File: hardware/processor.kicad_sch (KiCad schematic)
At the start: 9 parts, among them U801 RK3566

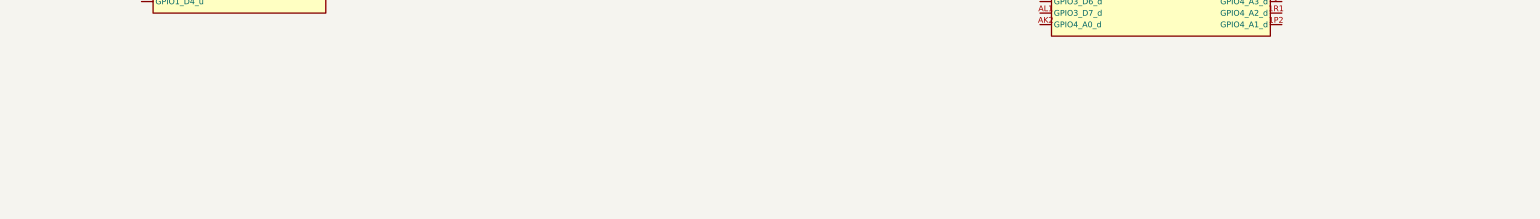
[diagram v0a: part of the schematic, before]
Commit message: Add local PMU logic and IO supply bypass capacitors
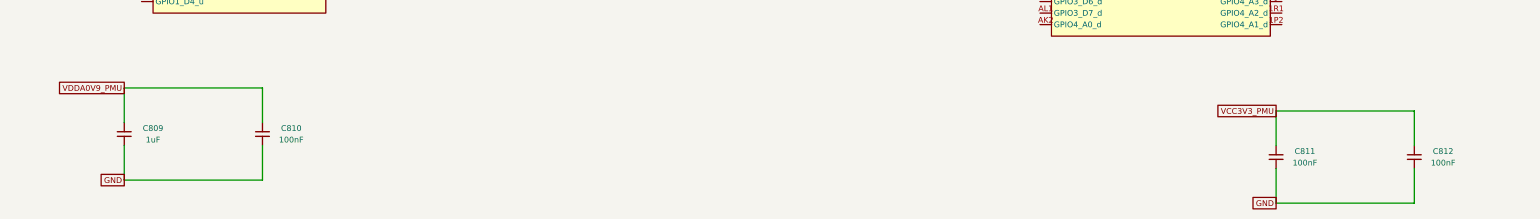
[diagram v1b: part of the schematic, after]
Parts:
- added C809: 1uF, Capacitor_SMD:C_0603_1608Metric, symbol Device:C_Small
- added C810, C811, C812: 100nF, Capacitor_SMD:C_0603_1608Metric, symbol Device:C_Small
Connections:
- net GND: now also C809.2, C810.2, C811.2, C812.2
- net VCC3V3_PMU: now also C811.1, C812.1
- net VDDA0V9_PMU: now also C809.1, C810.1

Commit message: Connect processor USB OTG and host analog supplies with local bypass
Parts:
- added C815, C816, C817: 100nF, Capacitor_SMD:C_0603_1608Metric, symbol Device:C_Small
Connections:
- net GND: now also C815.2, C816.2, C817.2
- net USB_AVDD_1V8: now reaches U801.1H16 (USB_AVDD1_1V8)
- net USB_AVDD_1V8: now also C816.1
- net 3V3_MAIN: now reaches U801.1H18 (USB_AVDD1_3V3)
- net 3V3_MAIN: now also C817.1
- net USB_AVDD_0V9: now reaches U801.1J17 (USB_AVDD1_0V9)
- net USB_AVDD_0V9: now also C815.1

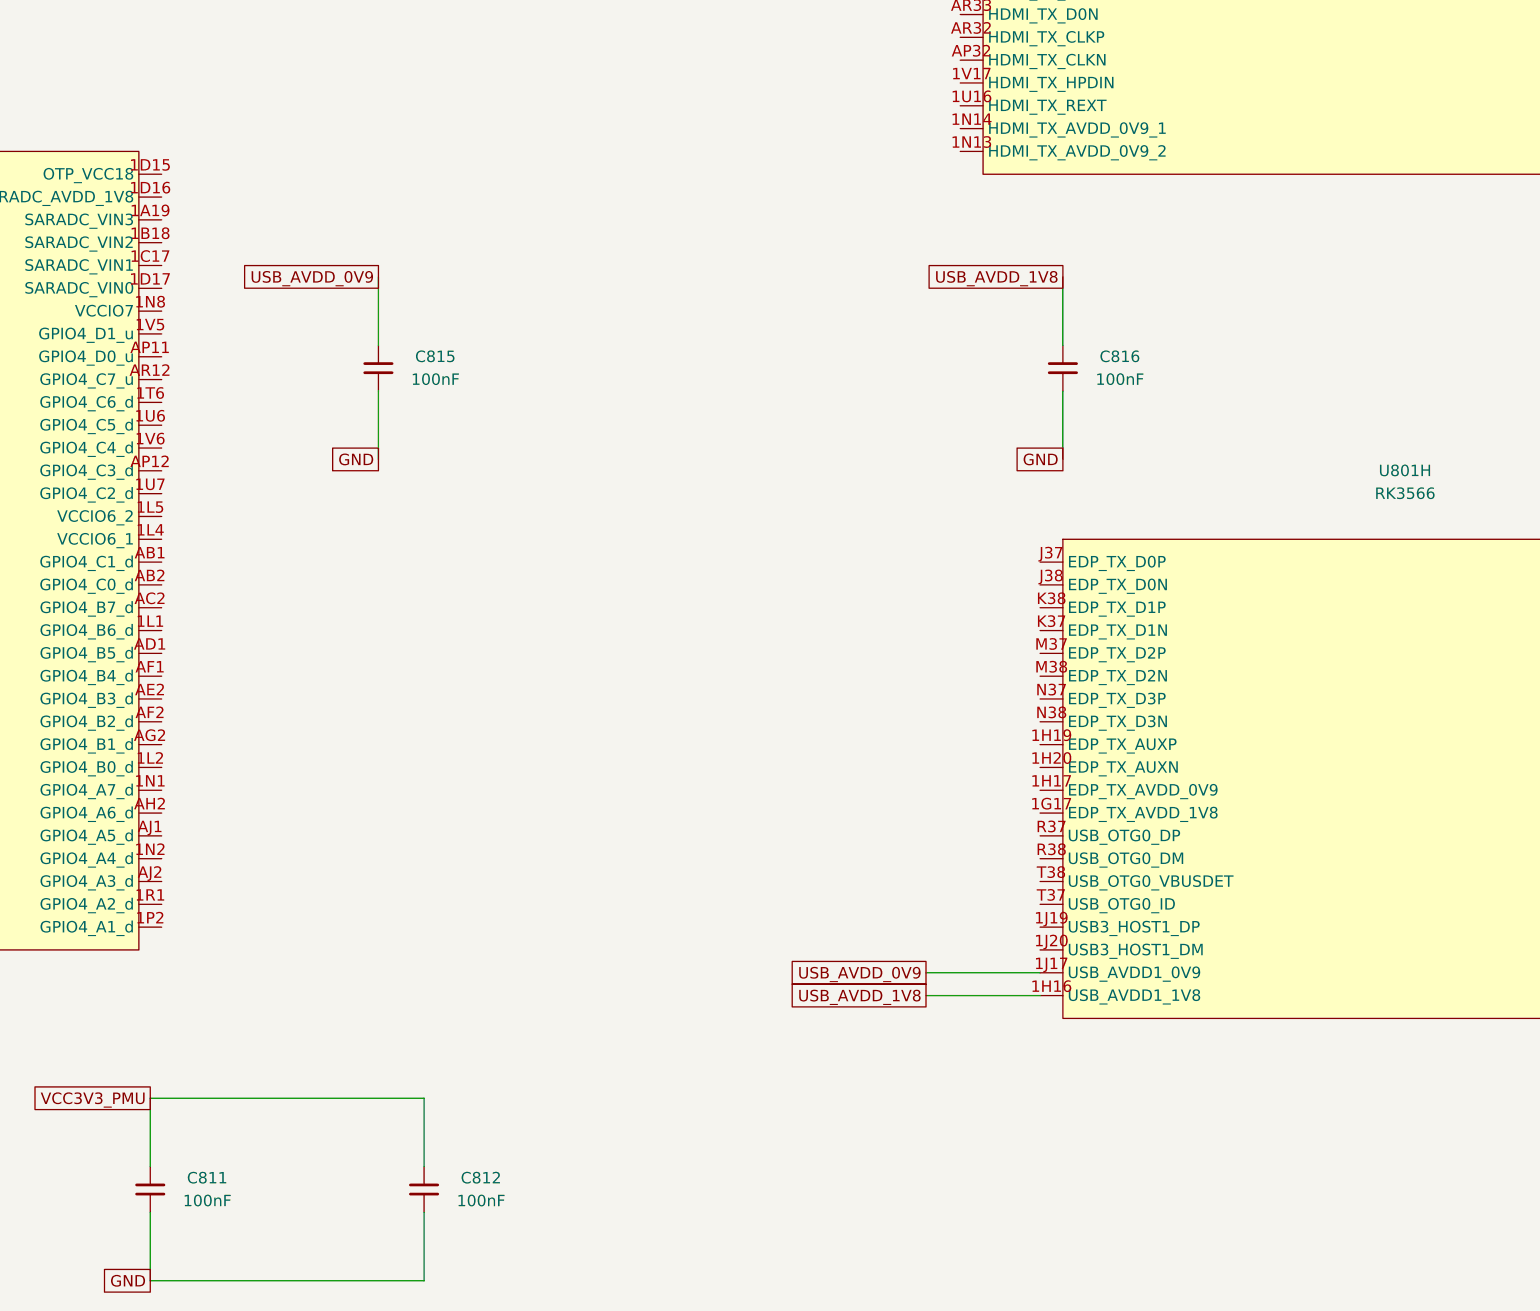
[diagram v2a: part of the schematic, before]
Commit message: Supply processor SARADC and OTP blocks with local bypass
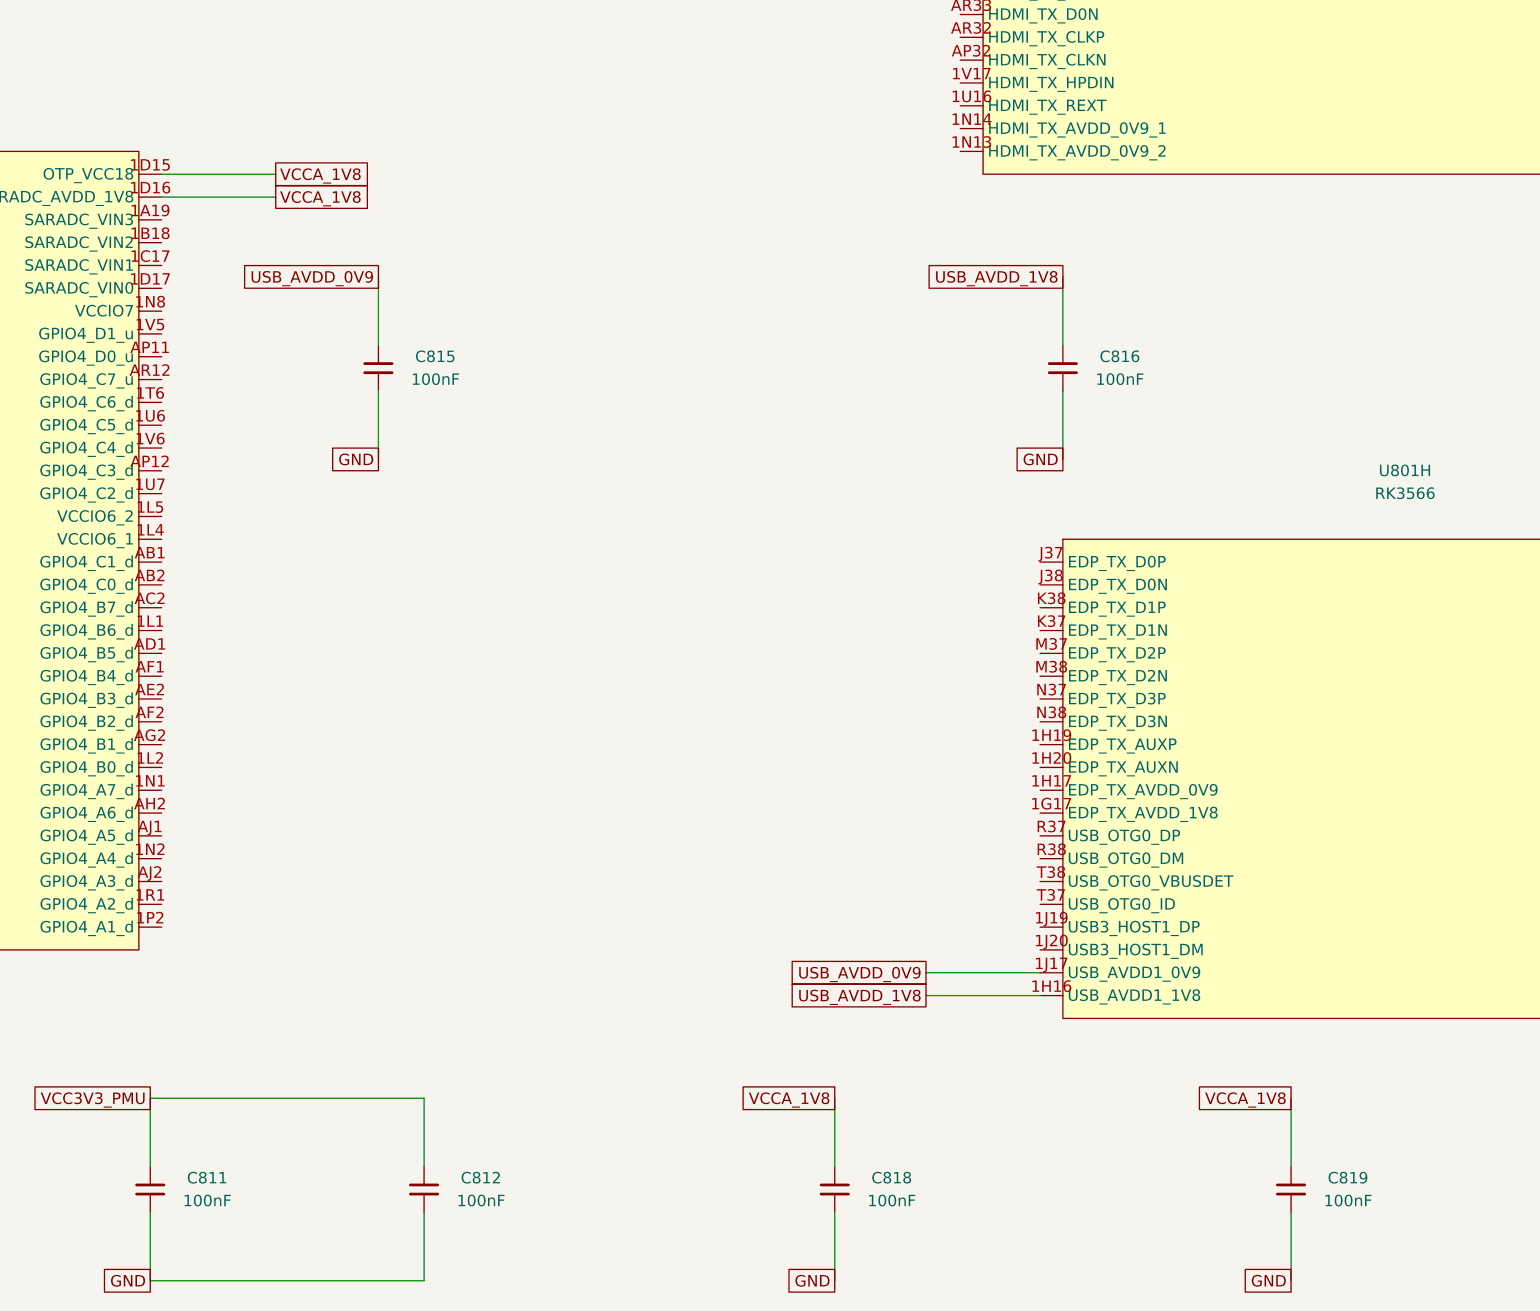
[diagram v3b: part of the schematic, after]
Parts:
- added C818, C819: 100nF, Capacitor_SMD:C_0603_1608Metric, symbol Device:C_Small
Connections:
- net GND: now also C818.2, C819.2
- net VCCA_1V8: now also U801.1D15 (OTP_VCC18), U801.1D16 (SARADC_AVDD_1V8), C818.1, C819.1

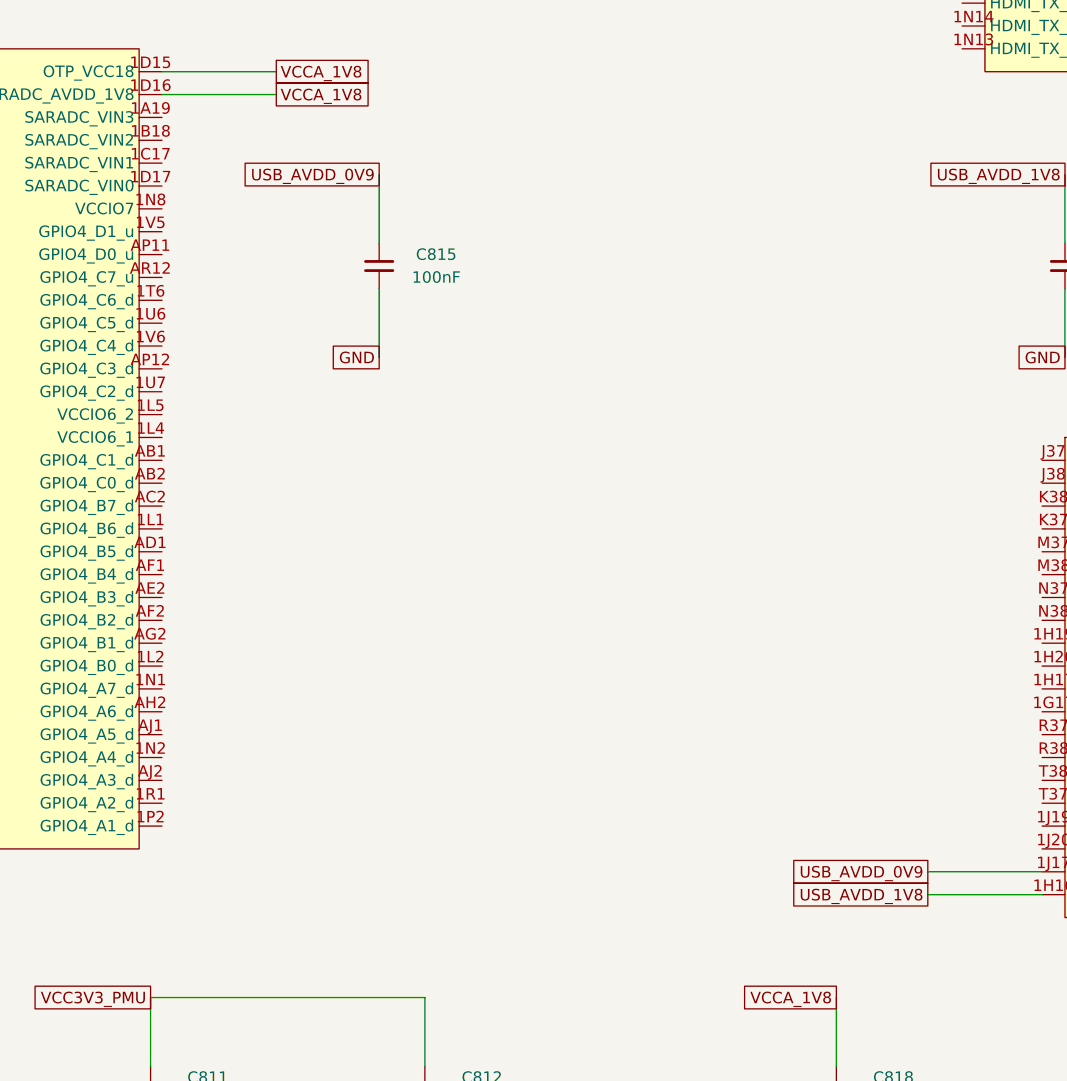
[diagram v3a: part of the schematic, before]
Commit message: Define processor SARADC normal boot input with pull-up and filter
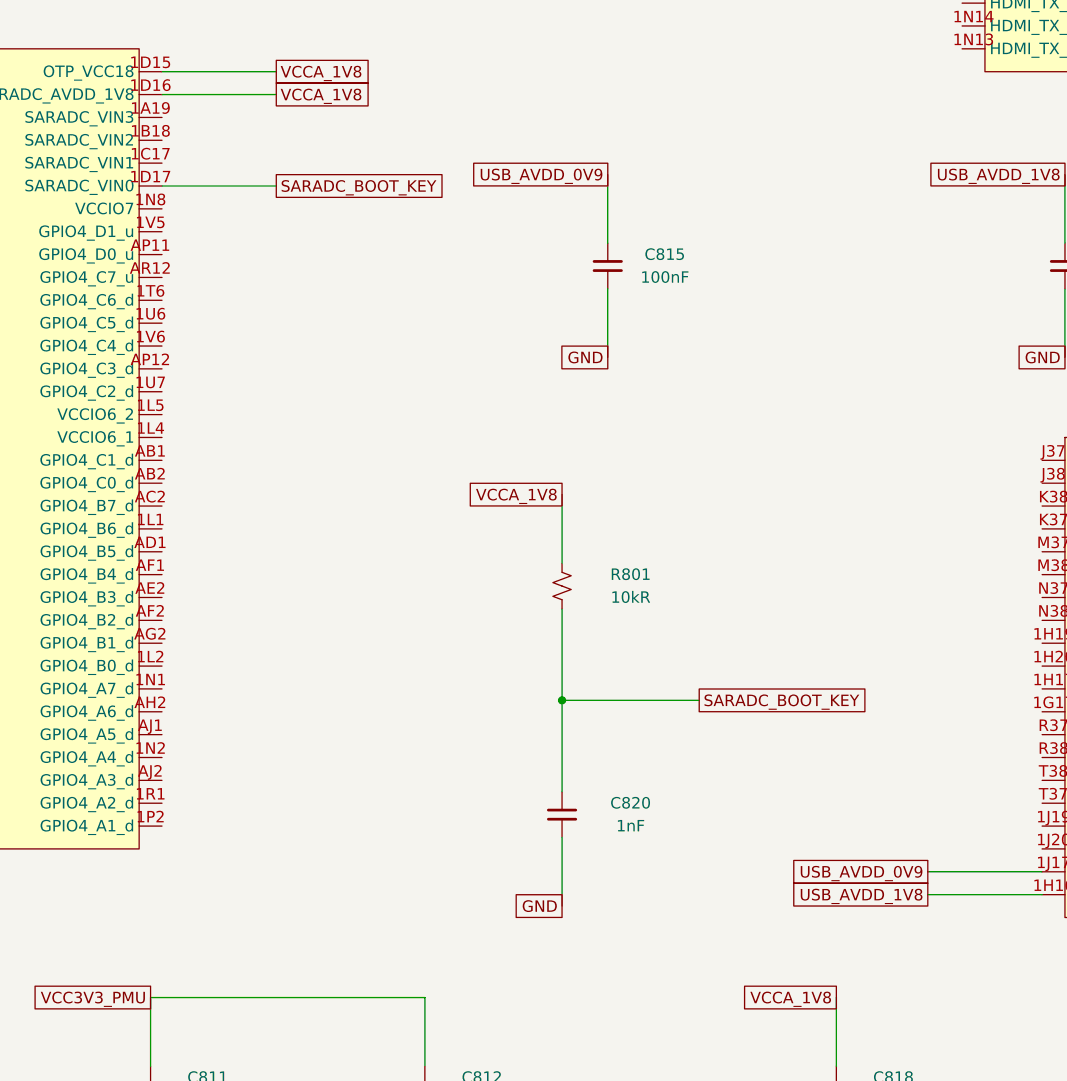
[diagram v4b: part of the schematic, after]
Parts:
- added C820: 1nF, Capacitor_SMD:C_0603_1608Metric, symbol Device:C_Small
- added R801: 10kR, Resistor_SMD:R_0603_1608Metric, symbol Device:R_Small_US
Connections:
- net GND: now also C820.2
- net VCCA_1V8: now also R801.1
- net SARADC_BOOT_KEY: now reaches U801.1D17 (SARADC_VIN0)
- net SARADC_BOOT_KEY: now also C820.1, R801.2
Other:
- moved on the sheet: C815

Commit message: Add manual processor Rockusb recovery request button
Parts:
- added SW801: PROCESSOR RECOVERY, Button_Switch_SMD:SW_SPST_TL3342, symbol Switch:SW_Push
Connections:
- net GND: now also SW801.2
- net SARADC_BOOT_KEY: now also SW801.1

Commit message: Add shared processor and PMIC reset button and clarify restart contract
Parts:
- removed SW801: PROCESSOR RECOVERY, Button_Switch_SMD:SW_SPST_TL3342, symbol Switch:SW_Push
- added SW802: PROCESSOR / PMIC RESET, Button_Switch_SMD:SW_SPST_TL3342, symbol Switch:SW_Push
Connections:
- net GND: now also SW802.2
- net RK_RESET_N: now also SW802.1
- net SARADC_BOOT_KEY: now also SW802.1

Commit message: Connect independent MCU processor and PMIC reset sink
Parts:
- added Q801: MMBT3904,215, Package_TO_SOT_SMD:SOT-23, symbol Transistor_BJT:MMBT3904
- added R802: 10kR, Resistor_SMD:R_0603_1608Metric, symbol Device:R_Small_US
- added R803: 100kR, Resistor_SMD:R_0603_1608Metric, symbol Device:R_Small_US
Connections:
- net GND: now also Q801.2 (E), R803.2
- net RK_RESET_N: now also Q801.3 (C)
- new net: Q801.1 (B), R802.2, R803.1
- new net MCU_PROCESSOR_RESET_ASSERT: R802.1

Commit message: Add independent MCU processor recovery request sink
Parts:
- added Q802: MMBT3904,215, Package_TO_SOT_SMD:SOT-23, symbol Transistor_BJT:MMBT3904
- added R804: 10kR, Resistor_SMD:R_0603_1608Metric, symbol Device:R_Small_US
- added R805: 100kR, Resistor_SMD:R_0603_1608Metric, symbol Device:R_Small_US
- Q801, R802, R803: Qualification Draft MCU-requested processor/PMIC restart; sink limits and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 -> Draft MCU-controlled reset sink; electrical limits and timi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
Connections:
- net GND: now also Q802.2 (E), R805.2
- net SARADC_BOOT_KEY: now also Q802.3 (C)
- new net: Q802.1 (B), R804.2, R805.1
- new net MCU_PROCESSOR_RECOVERY_ASSERT: R804.1
